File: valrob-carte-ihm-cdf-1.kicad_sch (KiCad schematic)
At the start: 0 parts

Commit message: schem: import ESP32-S3-WROOM-1 from valrob-carte-moteur-cdf-1
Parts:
- added C5: 1u, Capacitor_SMD:C_0603_1608Metric, symbol Device:C
- added C6: 22u, Capacitor_SMD:C_0805_2012Metric, symbol Device:C
- added C7: 0u1, Capacitor_SMD:C_0603_1608Metric, symbol Device:C
- added J4, J9: Conn_01x04_Pin, Connector_PinHeader_2.54mm:PinHeader_1x04_P2.54mm_Vertical, symbol Connector:Conn_01x04_Pin
- added R5: 10k, Resistor_SMD:R_0603_1608Metric, symbol Device:R
- added R8, R9: 22, Resistor_SMD:R_0603_1608Metric, symbol Device:R
- added U3: ESP32-S3-WROOM-1, PCM_Espressif:ESP32-S3-WROOM-1, symbol PCM_Espressif:ESP32-S3-WROOM-1
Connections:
- new net: J9.1 (Pin_1), U3.32 (MTCK/GPIO39/CLK_OUT3/SUBSPICS1)
- new net: J9.2 (Pin_2), U3.33 (MTDO/GPIO40/CLK_OUT2)
- new net: J9.3 (Pin_3), U3.34 (MTDI/GPIO41/CLK_OUT1)
- new net: J9.4 (Pin_4), U3.35 (MTMS/GPIO42)
- new net +3V3: C6.1, C7.1, J4.1 (Pin_1), R5.2, U3.2 (3V3)
- new net CHIP_PU: C5.2, R5.1, U3.3 (EN)
- new net D+: R8.2
- new net D-: R9.2
- new net ESP_D+: R8.1, U3.14 (GPIO20/U1CTS/ADC2_CH9/CLK_OUT1/USB_D+)
- new net ESP_D-: R9.1, U3.13 (GPIO19/U1RTS/ADC2_CH8/CLK_OUT2/USB_D-)
- new net GND: C5.1, C6.2, C7.2, J4.3 (Pin_3), U3.1 (GND), U3.40 (GND), U3.41 (GND)
- new net U0RXD: J4.2 (Pin_2), U3.36 (U0RXD/GPIO44/CLK_OUT2)
- new net U0TXD: J4.4 (Pin_4), U3.37 (U0TXD/GPIO43/CLK_OUT1)
- no-connect marks 0 -> 9
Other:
- note added: "EN RC delay"
- note added: "UART"

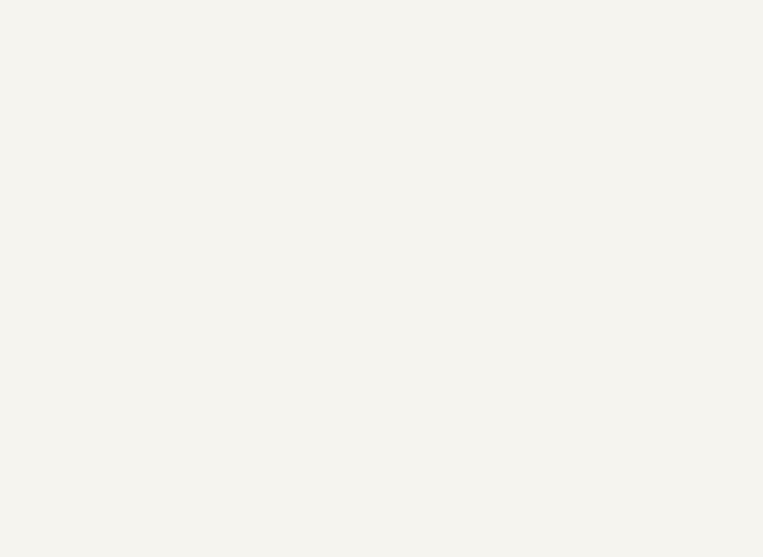
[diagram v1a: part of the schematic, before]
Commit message: schem: import USBC from valrob-carte-moteur-cdf-1
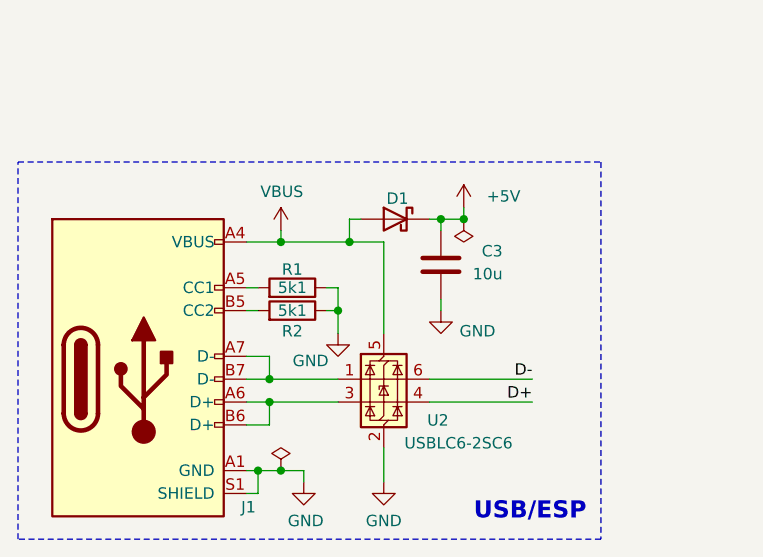
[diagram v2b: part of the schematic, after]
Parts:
- added C3: 10u, Capacitor_SMD:C_0603_1608Metric, symbol Device:C
- added D1: D_Schottky, Diode_SMD:D_SMA, symbol Device:D_Schottky
- added J1: USB_C_Receptacle_USB2.0_14P, Connector_USB:USB_C_Receptacle_HRO_TYPE-C-31-M-12, symbol Connector:USB_C_Receptacle_USB2.0_14P
- added R1, R2: 5k1, Resistor_SMD:R_0603_1608Metric, symbol Device:R
- added U2: USBLC6-2SC6, Package_TO_SOT_SMD:SOT-23-6, symbol Power_Protection:USBLC6-2SC6
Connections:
- net D+: now also U2.4 (I/O2)
- net D-: now also U2.6 (I/O1)
- net GND: now also C3.2, J1.A1 (GND), J1.A12 (GND), J1.B1 (GND), J1.B12 (GND), J1.S1 (SHIELD), R1.1, R2.1, U2.2 (GND)
- new net: J1.A5 (CC1), R1.2
- new net: J1.A6 (D+), J1.B6 (D+), U2.3 (I/O2)
- new net: J1.A7 (D-), J1.B7 (D-), U2.1 (I/O1)
- new net: J1.B5 (CC2), R2.2
- new net +5V: C3.1, D1.1 (K)
- new net VBUS: D1.2 (A), J1.A4 (VBUS), J1.A9 (VBUS), J1.B4 (VBUS), J1.B9 (VBUS), U2.5 (VBUS)
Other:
- note added: "USB/ESP"

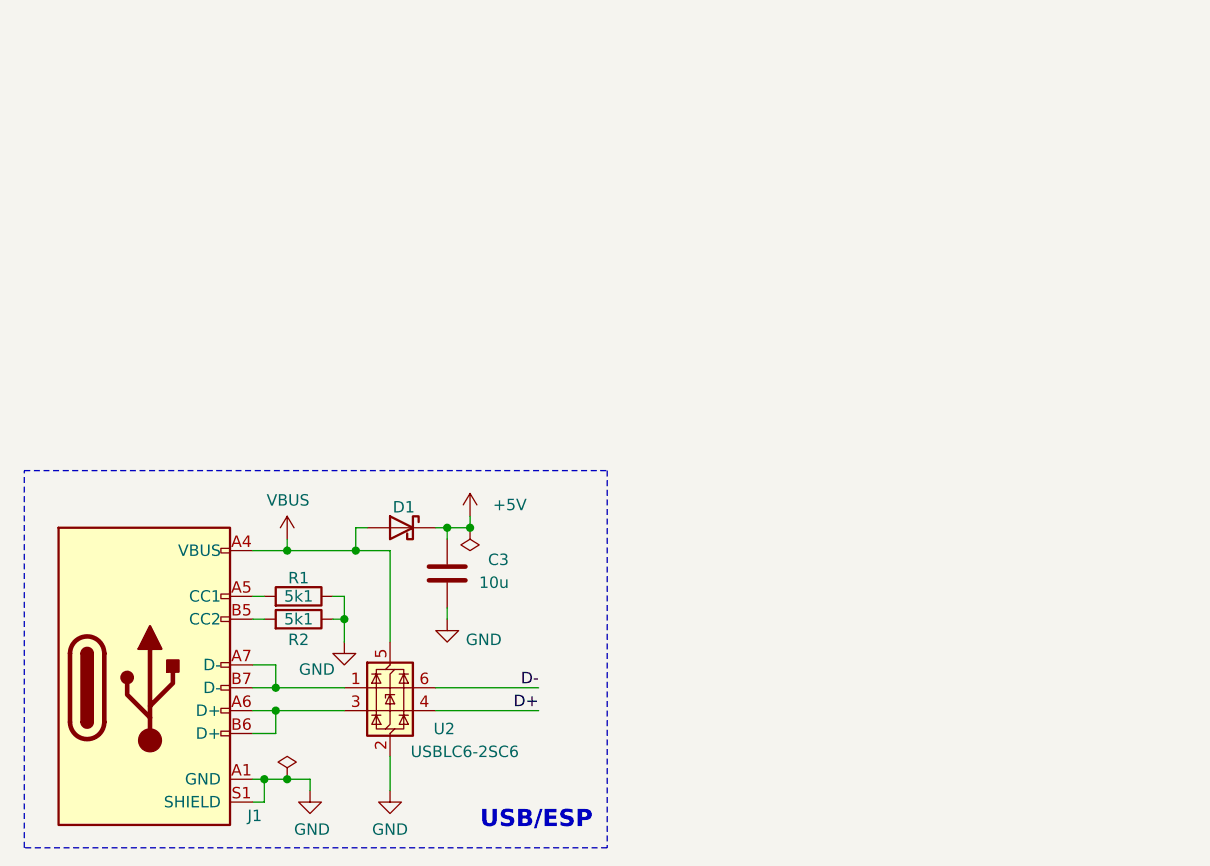
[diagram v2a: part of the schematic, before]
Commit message: schem: add TLV757P 3.3v LDO
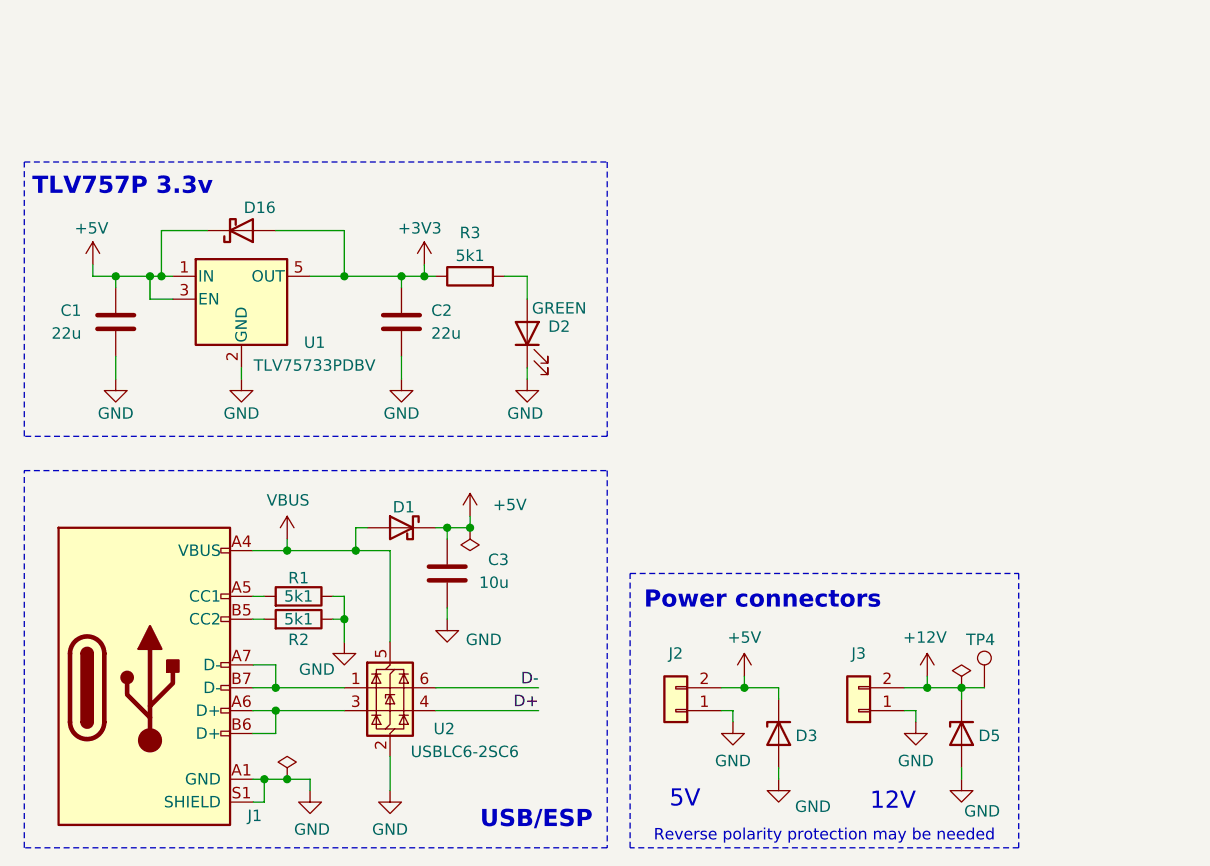
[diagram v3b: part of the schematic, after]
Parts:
- added C1, C2: 22u, symbol Device:C
- added D16: D_Schottky, Diode_SMD:D_SMA, symbol Device:D_Schottky
- added D2: GREEN, LED_SMD:LED_0805_2012Metric, symbol Device:LED
- added D3: P6SMB6.8CA/TR13, Diode_SMD:D_SMB, symbol Pers:H5VU10U
- added D5: SMAJ12A, Diode_SMD:D_SMA, symbol Pers:H5VU10U
- added J2, J3: Conn_01x02, Connector_JST:JST_XH_S2B-XH-A_1x02_P2.50mm_Horizontal, symbol Connector_Generic:Conn_01x02
- added R3: 5k1, Resistor_SMD:R_0603_1608Metric, symbol Device:R
- added TP4: TestPoint, TestPoint:TestPoint_Pad_D2.0mm, symbol Connector:TestPoint
- added U1: TLV75733PDBV, Package_TO_SOT_SMD:SOT-23-5, symbol Regulator_Linear:TLV75733PDBV
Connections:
- net +3V3: now also C2.2, D16.2 (A), R3.1, U1.5 (OUT)
- net +5V: now also C1.2, D16.1 (K), D3.1 (K), J2.2 (Pin_2), U1.1 (IN), U1.3 (EN)
- net GND: now also C1.1, C2.1, D2.1 (K), D3.2 (A), D5.2 (A), J2.1 (Pin_1), J3.1 (Pin_1), U1.2 (GND)
- new net: D2.2 (A), R3.2
- new net +12V: D5.1 (K), J3.2 (Pin_2), TP4.1
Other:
- note added: "12V"
- note added: "5V"
- note added: "Power connectors"
- note added: "Reverse polarity protection may be needed"
- note added: "TLV757P 3.3v"

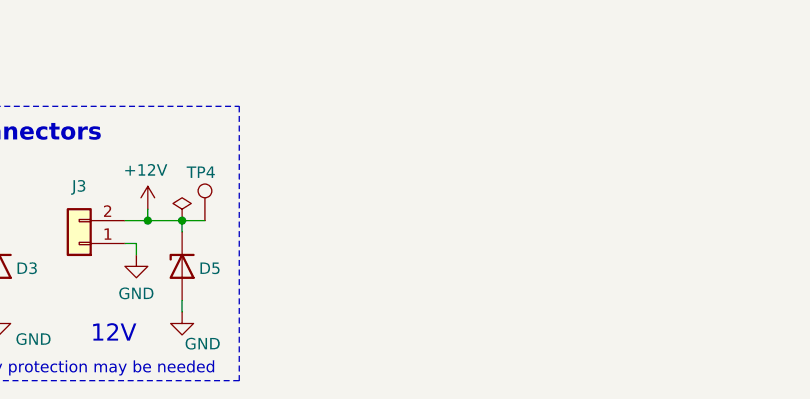
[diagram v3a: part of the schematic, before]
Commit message: schem: import BOOT and RST buttons from valrob-carte-moteur-cdf-1
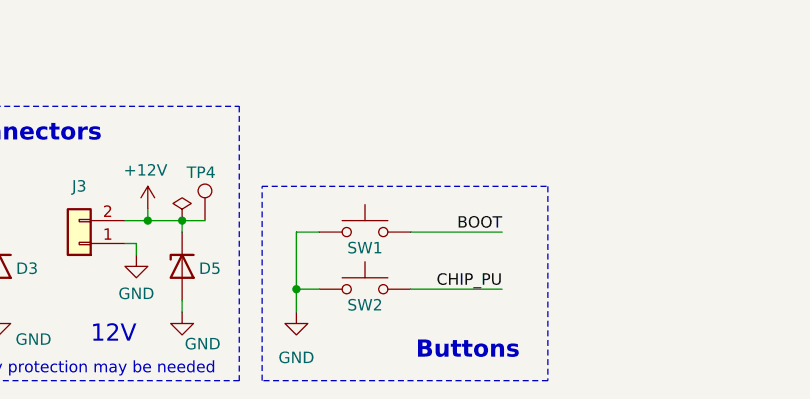
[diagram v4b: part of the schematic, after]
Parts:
- added SW1, SW2: SW_Push, Button_Switch_SMD:SW_SPST_TS-1088-xR020, symbol Switch:SW_Push
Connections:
- net CHIP_PU: now also SW2.2
- net GND: now also SW1.1, SW2.1
- new net BOOT: SW1.2
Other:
- note added: "Buttons"

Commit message: schem: add VBATT voltage sense
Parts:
- added C4: 0u1, Capacitor_SMD:C_0603_1608Metric, symbol Device:C
- added D4: BZT52B3V3, Diode_SMD:D_SOD-123, symbol Device:D
- added R4: 1k8, Resistor_SMD:R_0603_1608Metric, symbol Device:R
- added R6, R7: 10k, Resistor_SMD:R_0603_1608Metric, symbol Device:R
- added TP3: TestPoint, TestPoint:TestPoint_Pad_D2.0mm, symbol Connector:TestPoint
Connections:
- net +12V: now also R6.2; no longer D5.1 (K), J3.2 (Pin_2), TP4.1
- net BOOT: now also U3.27 (GPIO0/BOOT), R7.1
- net GND: now also C4.2, D4.2 (A), R4.2, R7.2
- net Vsense: now reaches U3.38 (GPIO2/TOUCH2/ADC1_CH1)
- net Vsense: now also C4.1, D4.1 (K), R4.1, R6.1, TP3.1
- new net +VBATT: D5.1 (K), J3.2 (Pin_2), TP4.1
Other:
- note added: "BATT"
- note added: "BATT sense"
- note removed: "12V"

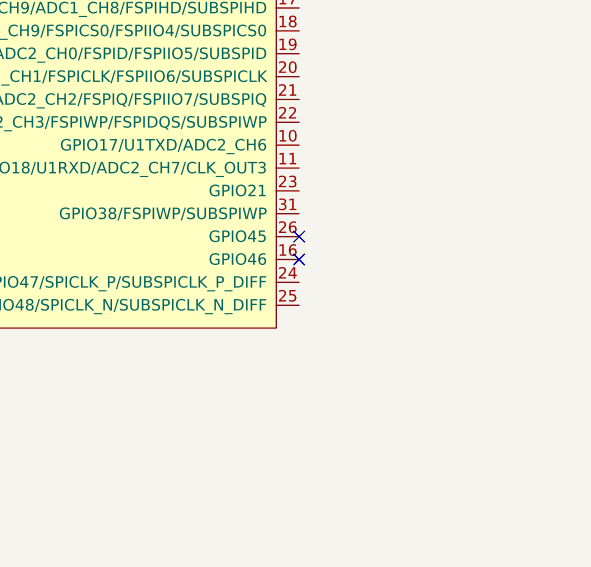
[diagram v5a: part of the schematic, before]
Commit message: schem: add dip switches
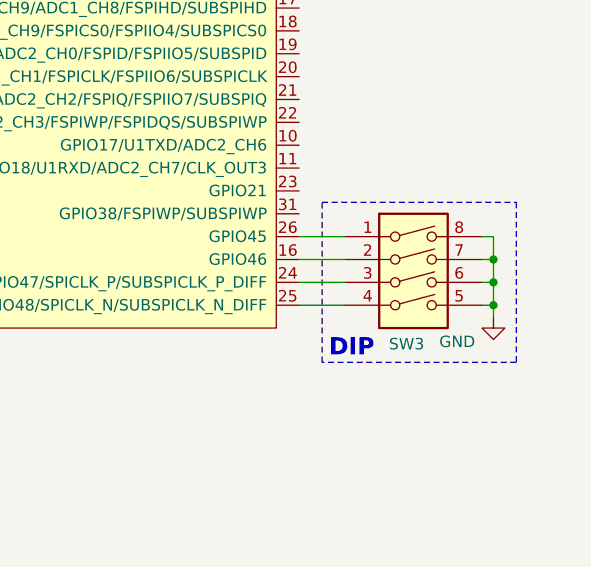
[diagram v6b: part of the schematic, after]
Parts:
- added SW3: SW_DIP_x04, Button_Switch_THT:SW_DIP_SPSTx04_Slide_9.78x12.34mm_W7.62mm_P2.54mm, symbol Switch:SW_DIP_x04
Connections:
- net GND: now also SW3.5, SW3.6, SW3.7, SW3.8
- net at U3.16 (GPIO46): now also SW3.2
- net at U3.24 (GPIO47/SPICLK_P/SUBSPICLK_P_DIFF): now also SW3.3
- net at U3.25 (GPIO48/SPICLK_N/SUBSPICLK_N_DIFF): now also SW3.4
- net at U3.26 (GPIO45): now also SW3.1
- no-connect marks 9 -> 7
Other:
- note added: "DIP"

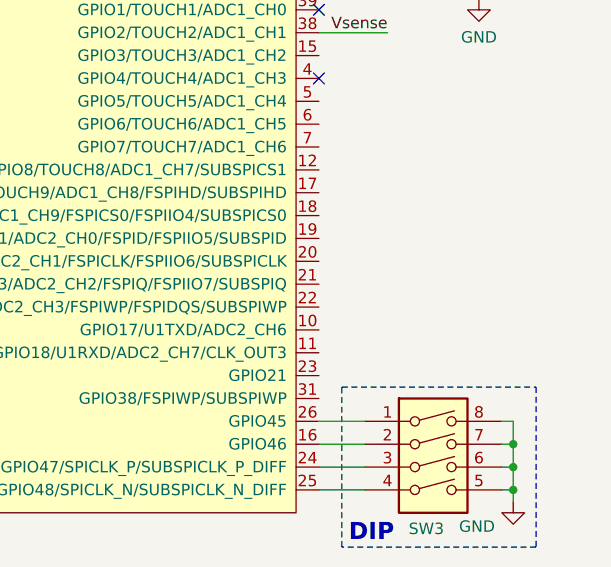
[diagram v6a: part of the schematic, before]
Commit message: schem: add debounced switches
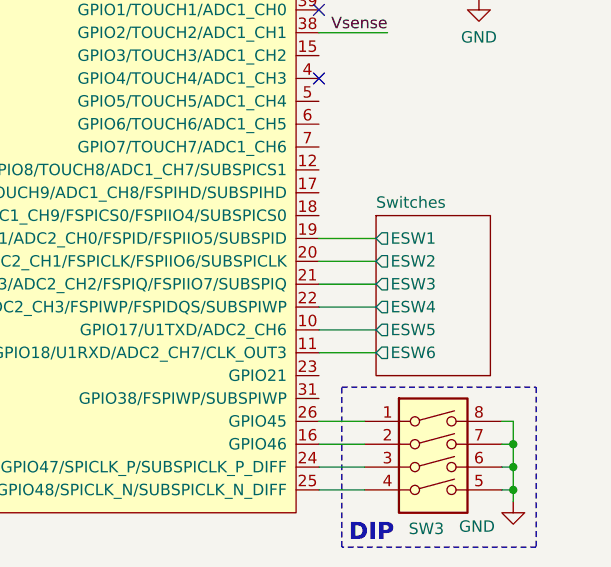
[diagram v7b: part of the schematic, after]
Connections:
- net Switches/ESW5: now reaches U3.10 (GPIO17/U1TXD/ADC2_CH6)
- net Switches/ESW6: now reaches U3.11 (GPIO18/U1RXD/ADC2_CH7/CLK_OUT3)
- net Switches/ESW1: now reaches U3.19 (GPIO11/TOUCH11/ADC2_CH0/FSPID/FSPIIO5/SUBSPID)
- net Switches/ESW2: now reaches U3.20 (GPIO12/TOUCH12/ADC2_CH1/FSPICLK/FSPIIO6/SUBSPICLK)
- net Switches/ESW3: now reaches U3.21 (GPIO13/TOUCH13/ADC2_CH2/FSPIQ/FSPIIO7/SUBSPIQ)
- net Switches/ESW4: now reaches U3.22 (GPIO14/TOUCH14/ADC2_CH3/FSPIWP/FSPIDQS/SUBSPIWP)
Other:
- added sheet Switches (Switches.kicad_sch)
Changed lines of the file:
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@@
 	(wire
 		(pts
+			(xy 246.38 102.87) (xy 252.73 102.87)
+		)
+		(stroke
+			(width 0)
+			(type default)
+		)
+	)
+	(wire
+		(pts
 			(xy 50.8 166.37) (xy 49.53 166.37)
 		)
@@
 	(wire
 		(pts
+			(xy 246.38 100.33) (xy 252.73 100.33)
+		)
+		(stroke
+			(width 0)
+			(type default)
+		)
+	)
+	(wire
+		(pts
 			(xy 25.4 130.81) (xy 25.4 132.08)
 		)
@@
 	(wire
 		(pts
+			(xy 246.38 113.03) (xy 252.73 113.03)
+		)
+		(stroke
+			(width 0)
+			(type default)
+		)
+	)
+	(wire
+		(pts
 			(xy 62.23 158.75) (xy 60.96 158.75)
 		)
@@
 	(wire
 		(pts
+			(xy 246.38 107.95) (xy 252.73 107.95)
+		)
+		(stroke
+			(width 0)
+			(type default)
+		)
+	)
+	(wire
+		(pts
 			(xy 55.88 161.29) (xy 52.07 161.29)
 		)
@@
 	(wire
 		(pts
+			(xy 246.38 110.49) (xy 252.73 110.49)
+		)
+		(stroke
+			(width 0)
+			(type default)
+		)
+	)
+	(wire
+		(pts
 			(xy 46.99 186.69) (xy 44.45 186.69)
 		)
@@
 	(wire
 		(pts
+			(xy 246.38 105.41) (xy 252.73 105.41)
+		)
+		(stroke
+			(width 0)
+			(type default)
+		)
+	)
+	(wire
+		(pts
 			(xy 25.4 130.81) (xy 22.86 130.81)
 		)
@@
 				)
 			)
+		)
+	)
+	(sheet
+		(at 252.73 97.79)
+		(size 12.7 17.78)
+		(exclude_from_sim no)
+		(in_bom yes)
+		(on_board yes)
+		(dnp no)
+		(fields_autoplaced yes)
+		(stroke
+			(width 0.1524)
+			(type solid)
+		)
+		(fill
+			(color 0 0 0 0.0000)
+		)
+		(property "Sheetname" "Switches"
+			(at 252.73 97.0784 0)
+			(effects
+				(font
+					(size 1.27 1.27)
+				)
+				(justify left bottom)
+			)
+		)
+		(property "Sheetfile" "Switches.kicad_sch"
+			(at 252.73 116.1546 0)
+			(effects
+				(font
+					(size 1.27 1.27)
+				)
+				(justify left top)
+				(hide yes)
+			)
+		)
+		(pin "ESW2" output
+			(at 252.73 102.87 180)
+			(effects
+				(font
+					(size 1.27 1.27)
+				)
+				(justify left)
+			)
+		)
+		(pin "ESW6" output
+			(at 252.73 113.03 180)
+			(effects
+				(font
+					(size 1.27 1.27)
+				)
+				(justify left)
+			)
+		)
+		(pin "ESW5" output
+			(at 252.73 110.49 180)
+			(effects
+				(font
+					(size 1.27 1.27)
+				)
+				(justify left)
+			)
+		)
+		(pin "ESW4" output
+			(at 252.73 107.95 180)
+			(effects
+				(font
+					(size 1.27 1.27)
+				)
+				(justify left)
+			)
+		)
+		(pin "ESW3" output
+			(at 252.73 105.41 180)
+			(effects
+				(font
+					(size 1.27 1.27)
+				)
+				(justify left)
+			)
+		)
+		(pin "ESW1" output
+			(at 252.73 100.33 180)
+			(effects
+				(font
+					(size 1.27 1.27)
+				)
+				(justify left)
+			)
+		)
+		(instances
+			(project "valrob-carte-ihm-cdf-1"
+				(path "/59430078-5c05-41f6-b5ab-2c89bd050ea6"
+					(page "2")
+				)
+			)

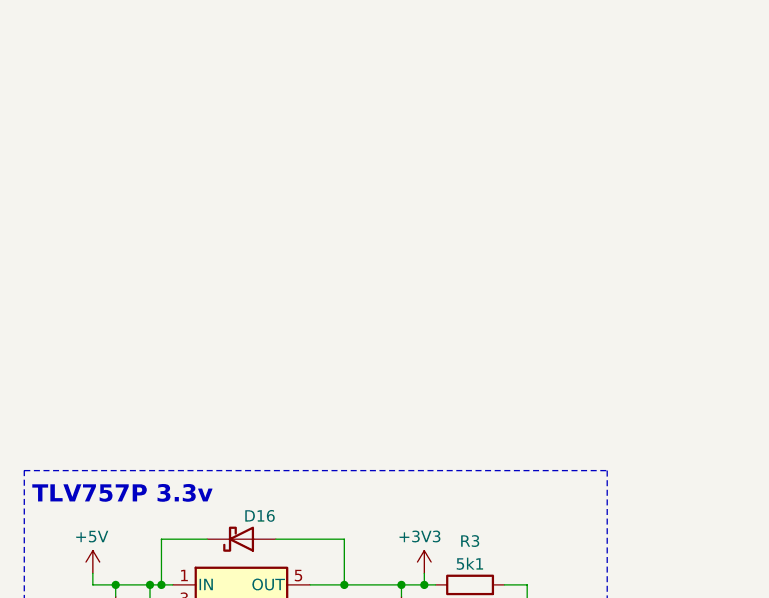
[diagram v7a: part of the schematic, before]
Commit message: schem: add WS2812B addressable RGB LEDs
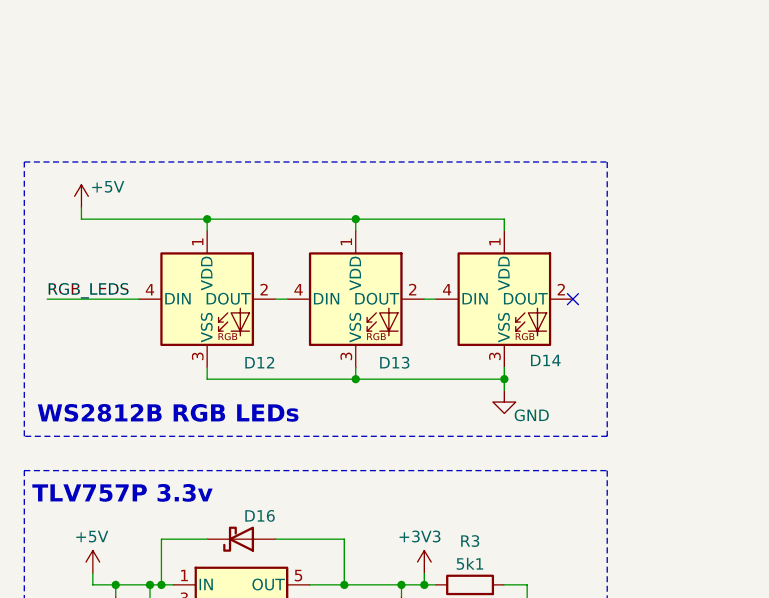
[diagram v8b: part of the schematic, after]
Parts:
- added D12, D13, D14: WS2812B, LED_SMD:LED_WS2812B_PLCC4_5.0x5.0mm_P3.2mm, symbol LED:WS2812B
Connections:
- net +5V: now also D12.1 (VDD), D13.1 (VDD), D14.1 (VDD)
- net GND: now also D12.3 (VSS), D13.3 (VSS), D14.3 (VSS)
- new net: D12.2 (DOUT), D13.4 (DIN)
- new net: D13.2 (DOUT), D14.4 (DIN)
- new net RGB_LEDS: D12.4 (DIN)
- no-connect marks 7 -> 8
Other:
- note added: "WS2812B RGB LEDs"
